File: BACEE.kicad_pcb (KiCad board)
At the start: 2 copper layers, 0 parts

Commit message: Set the design rules
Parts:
- added BT1: Battery 3V, Connector_PinHeader_2.54mm:PinHeader_1x02_P2.54mm_Vertical, F.Cu at (43.4, 38.1)
- added C1: 22pF, Capacitor_SMD:C_0805_2012Metric_Pad1.18x1.45mm_HandSolder, F.Cu at (27.4, 50.3)
- added C2: 22pF, Capacitor_SMD:C_0805_2012Metric_Pad1.18x1.45mm_HandSolder, F.Cu at (27.4, 55.5)
- added C3: 10uF, Capacitor_SMD:C_0805_2012Metric_Pad1.18x1.45mm_HandSolder, F.Cu at (27.4, 60.7)
- added D1: LED, LED_SMD:LED_0805_2012Metric_Pad1.15x1.40mm_HandSolder, F.Cu at (60.6, 61.7)
- added J1: Digital pins, Connector_PinSocket_2.54mm:PinSocket_1x09_P2.54mm_Vertical, F.Cu at (77.7, 31.5)
- added J2: Serial, Connector_PinSocket_2.54mm:PinSocket_1x04_P2.54mm_Vertical, F.Cu at (82.3, 31.5)
- added J3: ICSP, Connector_PinSocket_2.54mm:PinSocket_2x03_P2.54mm_Vertical, F.Cu at (87.3, 46.3)
- added J4: I2C, Connector_PinSocket_2.54mm:PinSocket_1x04_P2.54mm_Vertical, F.Cu at (86.9, 31.5)
- added R1: 330Ohm, Resistor_SMD:R_0805_2012Metric_Pad1.20x1.40mm_HandSolder, F.Cu at (60.7, 51.1)
- added R2: 10KOhm, Resistor_SMD:R_0805_2012Metric_Pad1.20x1.40mm_HandSolder, F.Cu at (60.7, 56.1)
- added U1: 24LC1025, Package_SO:SOIC-8_5.3x5.3mm_P1.27mm, F.Cu at (29.5, 30.9)
- added U2: 24LC1025, Package_SO:SOIC-8_5.3x5.3mm_P1.27mm, F.Cu at (29.3, 40.0)
- added U3: DS13375+, Package_SO:SOIC-8_3.9x4.9mm_P1.27mm, F.Cu at (43.0, 57.8)
- added U4: ATMEGA328-AU, digikey-footprints:TQFP-32_7x7mm, F.Cu at (61.7, 32.0)
- added Y1: 32MHz, Crystal:Crystal_SMD_MicroCrystal_CC7V-T1A-2Pin_3.2x1.5mm, F.Cu at (42.5, 51.6)
- added Y2: 16MHz, Crystal:Crystal_SMD_5032-2Pin_5.0x3.2mm_HandSoldering, F.Cu at (61.8, 41.7)

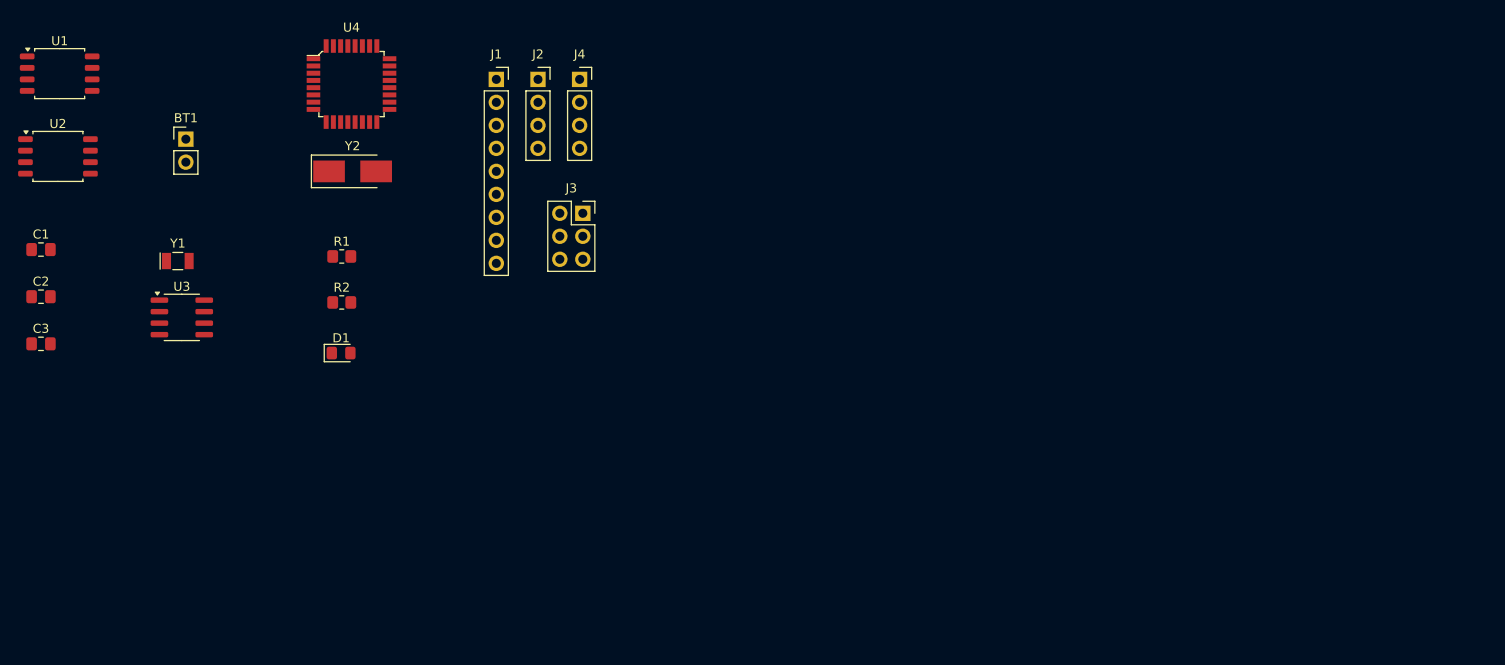
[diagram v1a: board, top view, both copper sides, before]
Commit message: Created outline and mounting holes.
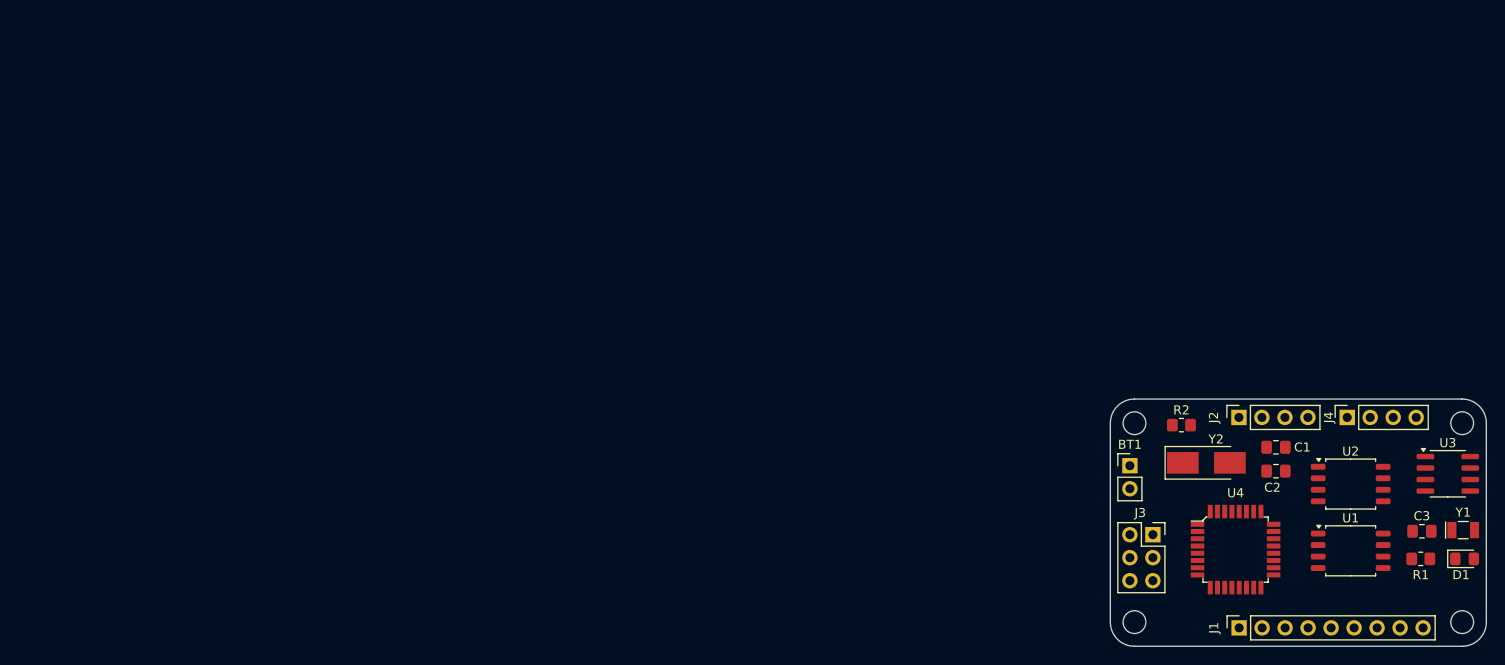
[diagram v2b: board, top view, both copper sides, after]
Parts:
- moved C3 153.9 mm to (180.0, 81.4)
- moved U1 152.0 mm to (172.1, 83.6)
- moved U2 147.3 mm to (172.1, 76.2)
- moved Y1 145.0 mm to (184.5, 81.3)
- moved U3 140.9 mm to (182.8, 75.1)
- moved C1 138.1 mm to (163.8, 72.1)
- moved C2 137.8 mm to (163.8, 74.8)
- moved D1 126.2 mm to (184.7, 84.5)
- moved R1 123.8 mm to (179.8, 84.5)
- moved U4 110.4 mm to (159.4, 83.4)
- moved BT1 110.3 mm to (147.7, 74.2)
- moved J1 102.0 mm to (159.8, 92.1), turned to 90 degrees
- moved Y2 99.6 mm to (156.1, 73.8)
- moved R2 93.7 mm to (153.4, 69.7)
- moved J4 92.6 mm to (171.7, 68.8), turned to 90 degrees
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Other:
- board outline added: 41.5 x 27.3 mm

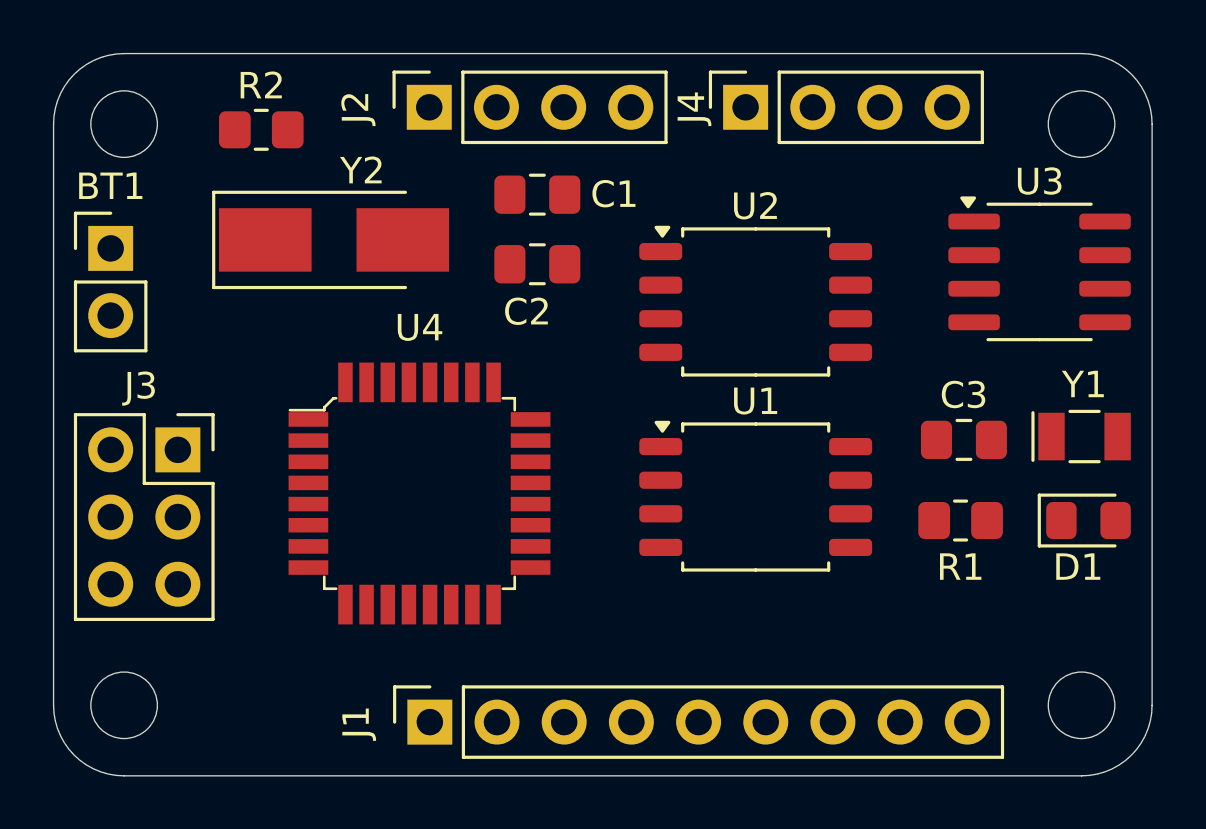
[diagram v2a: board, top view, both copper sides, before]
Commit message: Fully routed the board in 2 layers.
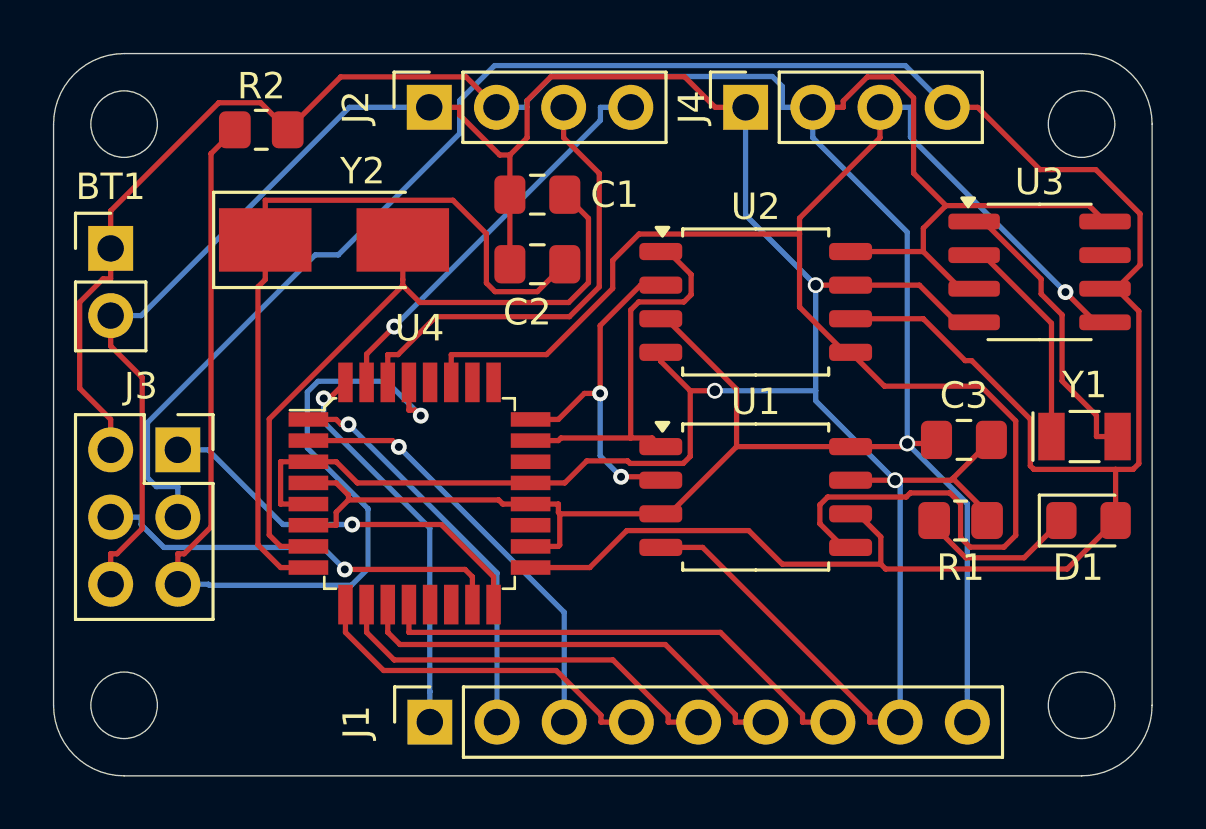
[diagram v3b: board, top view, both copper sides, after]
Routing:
- net /VCC: track 0.00 -> 126.6 mm, vias 0 -> 1
- net GNDPWR: track 0.00 -> 126.5 mm, vias 0 -> 3
- net /SCK: track 0.00 -> 104.2 mm
- net /SDA: track 0.00 -> 64.0 mm, vias 0 -> 1
- net /RESET: track 0.00 -> 39.9 mm, vias 0 -> 1
- net Net-(U4-PB7): track 0.00 -> 29.7 mm
- net Net-(U4-PB6): track 0.00 -> 26.2 mm
- net /D8: track 0.00 -> 18.7 mm
- net /RX: track 0.00 -> 17.5 mm
- net /D7: track 0.00 -> 16.9 mm
- net /D4: track 0.00 -> 16.5 mm, vias 0 -> 1
- net /MOSI: track 0.00 -> 15.8 mm, vias 0 -> 1
- net /TX: track 0.00 -> 15.2 mm, vias 0 -> 1
- net /D3: track 0.00 -> 15.2 mm, vias 0 -> 1
- net /D6: track 0.00 -> 15.2 mm
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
